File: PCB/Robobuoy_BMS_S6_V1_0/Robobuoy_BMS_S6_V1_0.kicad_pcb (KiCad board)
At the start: 4 copper layers, 147 parts, among them J101 Balance, J102 Balance, Q101 BFS20, Q102 MMBT5401, Q103 MMBT5401, Q104 MMBT5401, Q105 MMBT5401, Q106 MMBT5401, Q107 MMBT5401, Q108 MMBT5401, Q109 MMBT5401, Q110 MMBT5401, Q111 MMBT5401, Q112 MMBT5401, Q113 MMBT5401, Q114 BFS20, Q115 BFS20, Q116 HYG025N04NA1C2, Q117 HYG025N04NA1C2, Q118 HYG025N04NA1C2, Q119 HYG025N04NA1C2, U101 DW01A, U102 DW01A, U103 DW01A, U104 DW01A, U105 DW01A, U106 DW01A, U107 ETA3000D2I, U108 ETA3000D2I, U109 ETA3000D2I, U110 ETA3000D2I, U111 ETA3000D2I

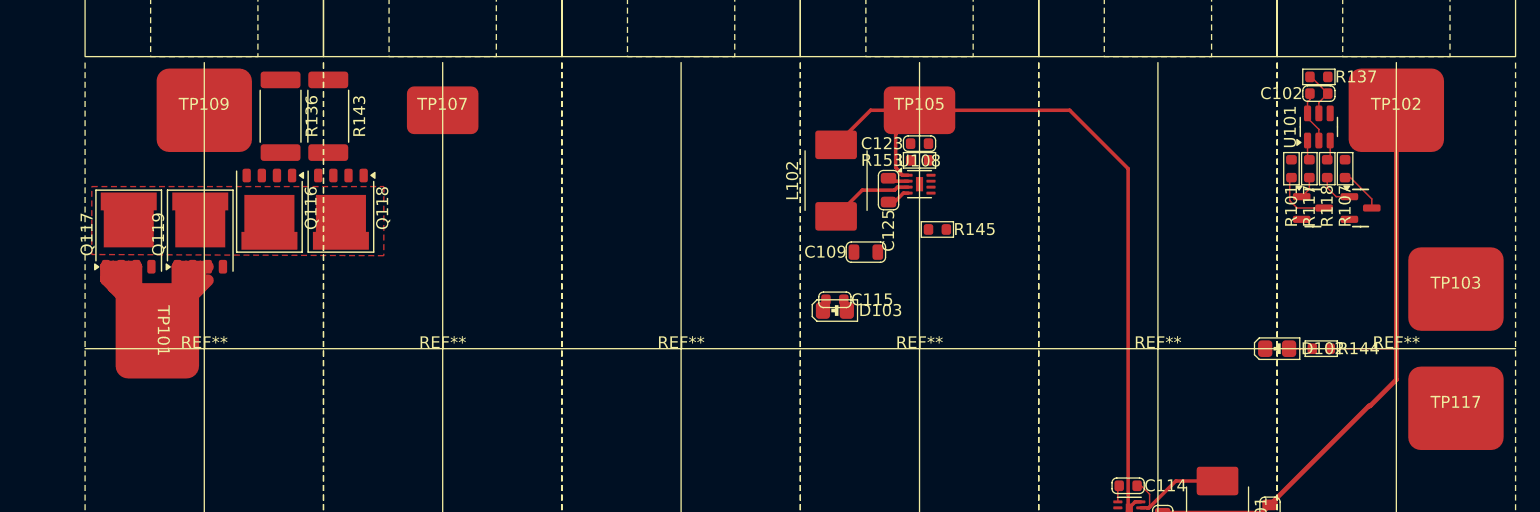
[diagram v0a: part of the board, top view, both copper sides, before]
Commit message: Schematics changed for singel board cpu/psu sub
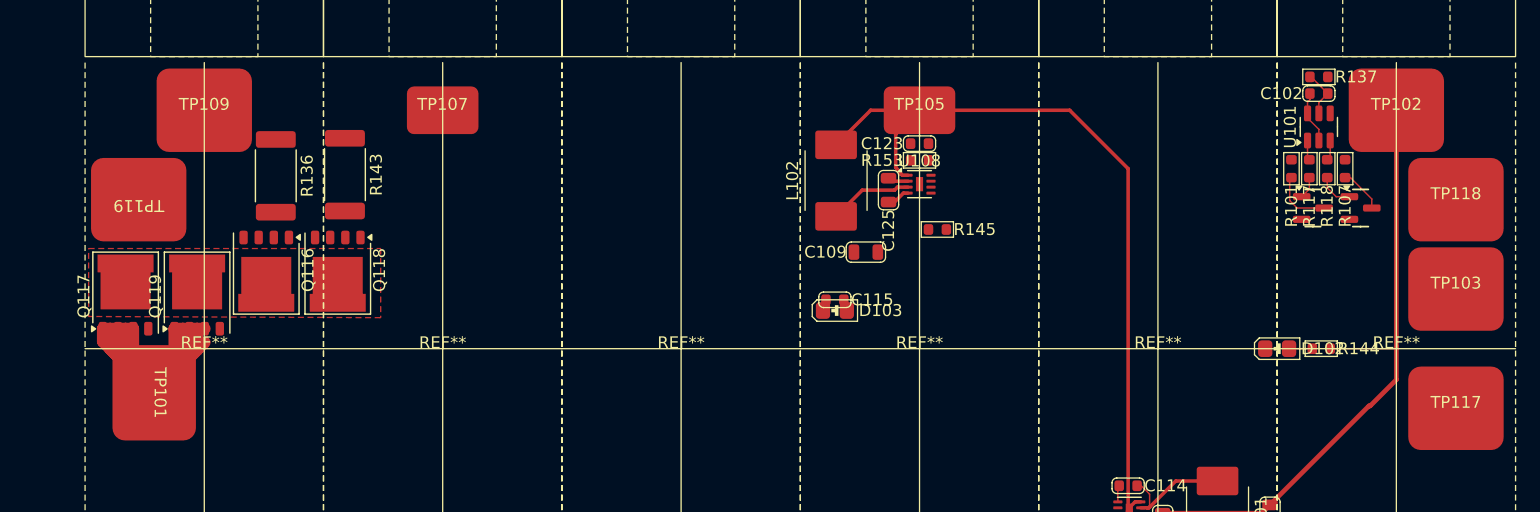
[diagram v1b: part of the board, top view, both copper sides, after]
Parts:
- added TP118: P+, A_Misc:TestPad_7x8, F.Cu at (165.0, 107.5)
- added TP119: B-, A_Misc:TestPad_7x8, F.Cu at (54.5, 107.5)
- moved TP101 5.21 mm to (55.8, 123.7)
- moved Q116 5.21 mm to (65.2, 113.4)
- moved Q118 5.21 mm to (71.2, 113.4)
- moved Q117 5.21 mm to (53.4, 115.6)
- moved Q119 5.21 mm to (59.4, 115.6)
- moved R143 5.10 mm to (71.8, 105.4)
- moved R136 5.02 mm to (66.0, 105.5)

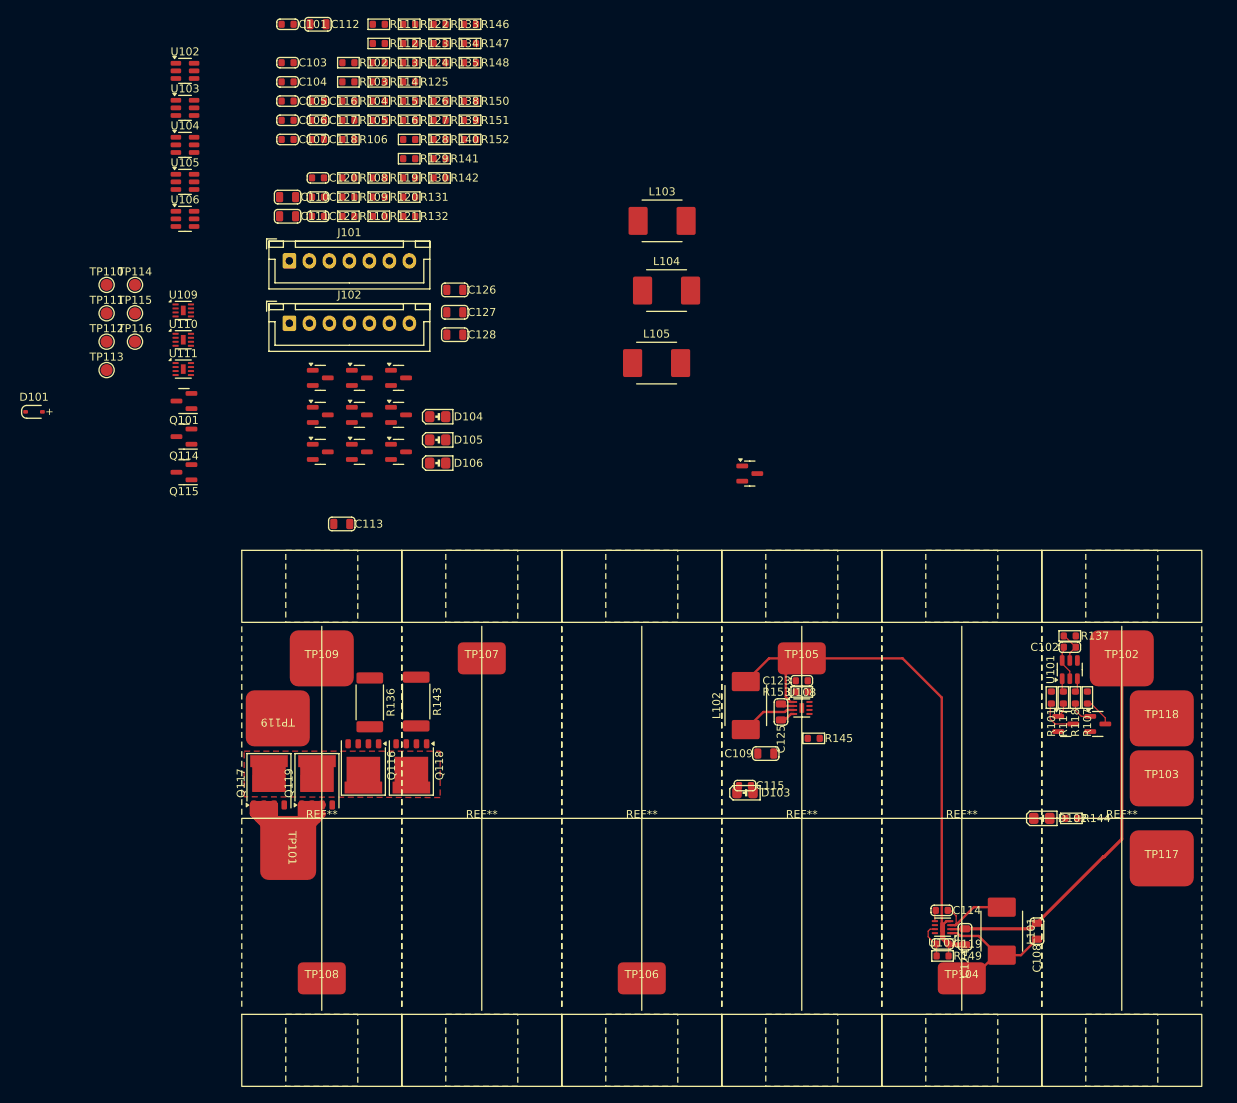
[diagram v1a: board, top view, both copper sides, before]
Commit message: Simulation added bms Little improvements BMS Resistor divider added on the gate of the mosfet (Limmeded to +/-20V could be 30V during charging)
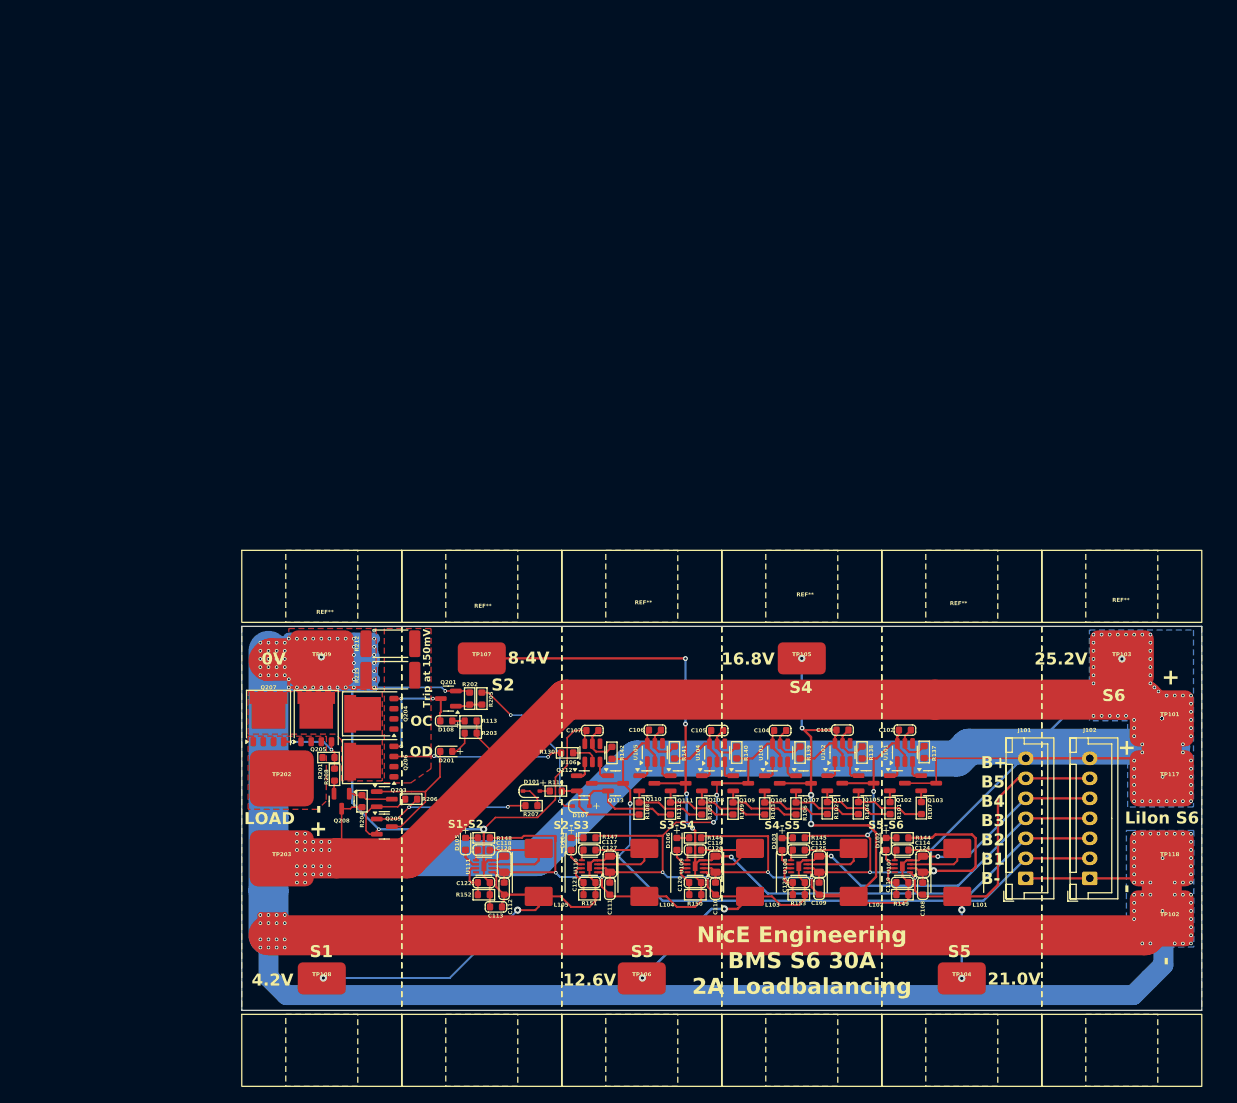
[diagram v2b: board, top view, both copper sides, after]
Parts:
- removed C101: 470nF, A_Device:C_0603
- removed Q101, Q114, Q115: BFS20, A_IC_SOT:SOT-23_jlc
- removed Q116, Q117, Q118, Q119: HYG025N04NA1C2, Package_DFN_QFN:PQFN-8-EP_6x5mm_P1.27mm_Generic
- removed R112, R114, R116, R117, R118, R119, R120, R121, R122, R123, R124, R125, R126, R127, R128, R129, R131, R132, R133, R135: 1M, A_Device:R_0603
- removed R115, R134: 10M, A_Device:R_0603
- removed R136, R143: R005, Resistor_SMD:R_2512_6332Metric_Pad1.40x3.35mm_HandSolder
- removed TP110: B+, TestPoint:TestPoint_Pad_D1.5mm
- removed TP111: B5, TestPoint:TestPoint_Pad_D1.5mm
- removed TP112: B4, TestPoint:TestPoint_Pad_D1.5mm
- removed TP113: B3, TestPoint:TestPoint_Pad_D1.5mm
- removed TP114: B2, TestPoint:TestPoint_Pad_D1.5mm
- removed TP115: B1, TestPoint:TestPoint_Pad_D1.5mm
- removed TP116: B-, TestPoint:TestPoint_Pad_D1.5mm
- removed TP119: B-, A_Misc:TestPad_7x8
- added D107: 1N4148WS, A_Device:D_SOD-323_1.8x1.4x1.15, F.Cu at (92.4, 118.5)
- added D108: RED, A_Device:LED_0603, F.Cu at (75.6, 107.8)
- added D201: RED, A_Device:LED_0603, F.Cu at (75.6, 111.6)
- added Q201: AO3400A, PCM_JLCPCB:Q_SOT-23, F.Cu at (75.8, 105.0)
- added Q203: AO3400A, PCM_JLCPCB:Q_SOT-23, F.Cu at (67.8, 117.6)
- added Q204: HYG025N04NA1C2, Package_DFN_QFN:PQFN-8-EP_6x5mm_P1.27mm_Generic, F.Cu at (66.3, 106.9)
- added Q205: HYG025N04NA1C2, Package_DFN_QFN:PQFN-8-EP_6x5mm_P1.27mm_Generic, F.Cu at (59.3, 107.7)
- added Q206: HYG025N04NA1C2, Package_DFN_QFN:PQFN-8-EP_6x5mm_P1.27mm_Generic, F.Cu at (66.3, 112.9)
- added Q207: HYG025N04NA1C2, Package_DFN_QFN:PQFN-8-EP_6x5mm_P1.27mm_Generic, F.Cu at (53.3, 107.7)
- added Q208: AO3400A, PCM_JLCPCB:Q_SOT-23, F.Cu at (62.5, 117.9)
- added Q209: AO3400A, PCM_JLCPCB:Q_SOT-23, F.Cu at (67.8, 121.0)
- added R201: 1M, A_Device:R_0603, F.Cu at (60.8, 112.4)
- added R202: 1M, A_Device:R_0603, F.Cu at (78.5, 105.0)
- added R203: 22K, A_Device:R_0603, F.Cu at (78.6, 109.3)
- added R204: 1M, A_Device:R_0603, F.Cu at (65.0, 117.9)
- added R205: 1K, A_Device:R_0603, F.Cu at (80.0, 105.0)
- added R206: 1M, A_Device:R_0603, F.Cu at (71.2, 117.6)
- added R207: 1K, A_Device:R_0603, F.Cu at (86.2, 118.4)
- added R208: 1M, A_Device:R_0603, F.Cu at (61.6, 114.5)
- added R212: R01, Resistor_SMD:R_2512_6332Metric_Pad1.40x3.35mm_HandSolder, F.Cu at (68.6, 98.2)
- added R213: R01, Resistor_SMD:R_2512_6332Metric_Pad1.40x3.35mm_HandSolder, F.Cu at (68.6, 102.1)
- added TP202: P-, A_Misc:TestPad_7x8, F.Cu at (55.0, 115.0)
- added TP203: P+, A_Misc:TestPad_7x8, F.Cu at (55.0, 125.0)
- C108, C109, C110, C111, C112, C113: footprint A_Device:C_0805 -> A_Device:C_0603
- D102: value 5-6 -> RED; footprint A_Passive:LED_0805 -> A_Device:LED_0603
- D103: value 4-5 -> RED; footprint A_Passive:LED_0805 -> A_Device:LED_0603
- D104: value 2-3 -> RED; footprint A_Passive:LED_0805 -> A_Device:LED_0603
- D105: value 1-2 -> RED; footprint A_Passive:LED_0805 -> A_Device:LED_0603
- D106: value 4-3 -> RED; footprint A_Passive:LED_0805 -> A_Device:LED_0603
- Q102, Q103, Q104, Q105, Q106, Q107, Q108, Q109, Q110, Q111, Q112, Q113: value MMBT5401 -> AO3400A
- R101, R102, R103, R104, R105, R106, R107, R108, R109, R110, R111: value 1M -> 1K
- R113: value 1M -> 22K
- R137, R138, R139, R140, R141, R142: value 1k -> 100
- R144, R145, R146, R147, R148: value 1k -> 1K
- R149, R150, R151, R152, R153: value 25K -> 24K
- TP101, TP117: value P- -> VBATT+
- TP102, TP118: value P+ -> VBATT-
- moved J102 121.8 mm to (156.0, 127.5), turned to 90 degrees
- moved J101 120.1 mm to (148.0, 127.5), turned to 90 degrees
- moved U102 118.4 mm to (125.1, 111.8), turned to 90 degrees
- moved TP101 111.4 mm to (166.0, 107.5), turned to 0 degrees
- moved R102 110.8 mm to (123.2, 118.7), turned to 90 degrees
- moved C112 110.5 mm to (82.8, 128.8), turned to -90 degrees
- moved U103 109.7 mm to (117.3, 111.8), turned to 90 degrees
- moved R104 109.0 mm to (127.1, 118.7), turned to 90 degrees
- moved C103 108.5 mm to (125.1, 109.0), turned to 180 degrees
- moved R146 105.5 mm to (106.7, 122.4)
- moved C116 104.8 mm to (106.7, 124.0)
- moved R103 104.7 mm to (115.4, 118.8), turned to 90 degrees
- moved R111 104.6 mm to (103.6, 118.8), turned to 90 degrees
- moved R150 103.1 mm to (106.7, 129.5)
- moved C104 101.8 mm to (117.3, 109.0), turned to 180 degrees
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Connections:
- D101 pad 1: Net-(D101-K) -> /Curren-Overcharge-Protection/OD
- Q102 pad 1: Net-(Q102-B) -> Net-(Q102-G)
- Q102 pad 2: VBATT+ -> Net-(Q102-S)
- Q102 pad 3: Net-(Q102-C) -> VBATT+
- Q103 pad 1: Net-(Q103-B) -> Net-(Q103-G)
- Q103 pad 2: VBATT+ -> Net-(Q103-S)
- Q103 pad 3: Net-(Q103-C) -> VBATT+
- Q104 pad 1: Net-(Q104-B) -> Net-(Q104-G)
- Q104 pad 2: /B5 -> Net-(Q104-S)
- Q104 pad 3: Net-(Q104-C) -> /B5
- Q105 pad 1: Net-(Q105-B) -> Net-(Q105-G)
- Q105 pad 2: /B5 -> Net-(Q105-S)
- Q105 pad 3: Net-(Q105-C) -> /B5
- Q106 pad 1: Net-(Q106-B) -> Net-(Q106-G)
- Q106 pad 2: /B4 -> Net-(Q106-S)
- Q106 pad 3: Net-(Q106-C) -> /B4
- Q107 pad 1: Net-(Q107-B) -> Net-(Q107-G)
- Q107 pad 2: /B4 -> Net-(Q107-S)
- Q107 pad 3: Net-(Q107-C) -> /B4
- Q108 pad 1: Net-(Q108-B) -> Net-(Q108-G)
- Q108 pad 2: /B3 -> Net-(Q108-S)
- Q108 pad 3: Net-(Q108-C) -> /B3
- Q109 pad 1: Net-(Q109-B) -> Net-(Q109-G)
- Q109 pad 2: /B3 -> Net-(Q109-S)
- Q109 pad 3: Net-(Q109-C) -> /B3
- Q110 pad 1: Net-(Q110-B) -> Net-(Q110-G)
- Q110 pad 2: /B2 -> Net-(Q110-S)
- Q110 pad 3: Net-(Q110-C) -> /B2
- Q111 pad 1: Net-(Q111-B) -> Net-(Q111-G)
- Q111 pad 2: /B2 -> Net-(Q111-S)
- Q111 pad 3: Net-(Q111-C) -> /B2
- Q112 pad 1: Net-(Q112-B) -> Net-(Q112-G)
- Q112 pad 2: /B1 -> Net-(Q112-S)
- Q112 pad 3: Net-(Q112-C) -> /B1
- Q113 pad 1: Net-(Q113-B) -> Net-(Q113-G)
- Q113 pad 2: /B1 -> Net-(D107-A)
- Q113 pad 3: Net-(Q113-C) -> /B1
- R101 pad 1: Net-(Q104-C) -> Net-(Q104-S)
- R101 pad 2: Net-(Q102-C) -> Net-(Q102-S)
- R102 pad 1: Net-(Q106-C) -> Net-(Q106-S)
- R102 pad 2: Net-(Q104-C) -> Net-(Q104-S)
- R103 pad 1: Net-(Q108-C) -> Net-(Q108-S)
- R103 pad 2: Net-(Q106-C) -> Net-(Q106-S)
- R104 pad 1: Net-(Q110-C) -> Net-(Q107-S)
- R104 pad 2: Net-(Q108-C) -> Net-(Q105-S)
- R105 pad 1: Net-(Q112-C) -> Net-(Q110-S)
- R105 pad 2: Net-(Q110-C) -> Net-(Q108-S)
- R106 pad 1: Net-(D101-A) -> Net-(Q109-S)
- R106 pad 2: Net-(Q112-C) -> Net-(Q107-S)
- R107 pad 1: Net-(Q105-C) -> Net-(Q105-S)
- R107 pad 2: Net-(Q103-C) -> Net-(Q103-S)
- R108 pad 1: Net-(Q107-C) -> Net-(Q112-S)
- R108 pad 2: Net-(Q105-C) -> Net-(Q110-S)
- R109 pad 1: Net-(Q109-C) -> Net-(Q111-S)
- R109 pad 2: Net-(Q107-C) -> Net-(Q109-S)
- R110 pad 1: Net-(Q111-C) -> Net-(D101-A)
- R110 pad 2: Net-(Q109-C) -> Net-(Q112-S)
- R111 pad 1: Net-(Q113-C) -> Net-(D107-A)
- R111 pad 2: Net-(Q111-C) -> Net-(Q111-S)
- R113 pad 1: VBATT- -> Net-(D108-A)
- R113 pad 2: Net-(Q101-B) -> VBATT+
- R130 pad 1: Net-(Q116-S-Pad1) -> /Curren-Overcharge-Protection/Vtrip
- TP101 pad 1: /P- -> VBATT+
- TP102 pad 1: VBATT+ -> VBATT-
- TP117 pad 1: /P- -> VBATT+
- TP118 pad 1: VBATT+ -> VBATT-
- U101 pad 1: Net-(U101-OD) -> Net-(Q102-G)
- U101 pad 3: Net-(U101-OC) -> Net-(Q103-G)
- U102 pad 1: Net-(U102-OD) -> Net-(Q104-G)
- U102 pad 3: Net-(U102-OC) -> Net-(Q105-G)
- U103 pad 1: Net-(U103-OD) -> Net-(Q106-G)
- U103 pad 3: Net-(U103-OC) -> Net-(Q107-G)
- U104 pad 1: Net-(U104-OD) -> Net-(Q108-G)
- U104 pad 3: Net-(U104-OC) -> Net-(Q109-G)
- U105 pad 1: Net-(U105-OD) -> Net-(Q110-G)
- U105 pad 3: Net-(U105-OC) -> Net-(Q111-G)
- U106 pad 1: Net-(U106-OD) -> Net-(Q112-G)
- U106 pad 3: Net-(U106-OC) -> Net-(Q113-G)
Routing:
- net VBATT-: track 0.00 -> 502.3 mm, vias 0 -> 117
- net VBATT+: track 54.3 -> 384.7 mm, vias 0 -> 93
- net /B2: track 0.00 -> 169.5 mm, vias 0 -> 7
- net /B1: track 0.00 -> 147.9 mm, vias 0 -> 4
- net /B3: track 1.95 -> 136.7 mm, vias 0 -> 7
- net /B5: track 25.2 -> 97.4 mm, vias 0 -> 6
- net /P-: track 70.2 -> 0.00 mm
- net /B4: track 70.9 -> 138.0 mm, vias 0 -> 7
- net /Curren-Overcharge-Protection/Vtrip: track 0.00 -> 21.2 mm, vias 0 -> 2
- net /Curren-Overcharge-Protection/OC: track 0.00 -> 20.7 mm, vias 0 -> 2
- net Net-(Q209-G): track 0.00 -> 20.7 mm, vias 0 -> 2
- net Net-(D201-K): track 0.00 -> 18.6 mm
- net Net-(D108-K): track 0.00 -> 15.6 mm, vias 0 -> 3
- net Net-(D107-A): track 0.00 -> 13.7 mm
- net Net-(U110-SW): track 0.00 -> 13.5 mm
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- added copper zone on F.Cu, net /Curren-Overcharge-Protection/P-
- added copper zone on F.Cu, net /Curren-Overcharge-Protection/Vtrip
- added copper zone on F.Cu, net Net-(Q204-D)
- added copper zone on B.Cu, net VBATT+
- added copper zone on In2.Cu, net VBATT+
- added copper zone on B.Cu, net VBATT-
- added copper zone on F.Cu, net VBATT-
- added copper zone on In1.Cu, net VBATT-
- removed copper zone on F.Cu, net Net-(Q116-D)
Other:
- board outline added: 120 x 48 mm
- board text added: "+"
- board text added: "-"
- board text added: "0V"
- board text added: "12.6V"
- board text added: "16.8V"
- board text added: "21.0V"
- board text added: "25.2V"
- board text added: "4.2V"
- board text added: "8.4V"
- board text added: "B+ B5 B4 B3 B2 B1 B-"
- board text added: "LOAD"
- board text added: "LiIon S6"
- board text added: "NicE Engineering BMS S6 30A 2A Active loadbalancing"
- board text added: "NicE Engineering BMS S6 30A 2A Loadbalancing"
- board text added: "S1"
- board text added: "S1-S2"
- board text added: "S2"
- board text added: "S2-S3"
- board text added: "S3"
- board text added: "S3-S4"
- board text added: "S4"
- board text added: "S4-S5"
- board text added: "S5"
- board text added: "S5-S6"
- board text added: "S6"
- board text added: "Trip at 150mV"

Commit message: PCB adjustmend Sub V3.0
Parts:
- added TP110: B1, A_Misc:TestPad_4x6, F.Cu at (76.6, 140.2)
- added TP111: B2, A_Misc:TestPad_4x6, F.Cu at (101.7, 99.3)
- added TP112: B3, A_Misc:TestPad_4x6, F.Cu at (120.0, 140.0)
- added TP113: B4, A_Misc:TestPad_4x6, F.Cu at (140.0, 100.0)
- added TP114: B5, A_Misc:TestPad_4x6, F.Cu at (160.0, 140.0)
- R208: value 1M -> 10K
- turned R208 to -90 degrees
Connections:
- R208 pad 1: Net-(Q208-S) -> Net-(Q205-G)
- R208 pad 2: Net-(Q205-G) -> Net-(Q208-S)
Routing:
- net /B5: track 97.4 -> 117.4 mm
- net /B4: track 138.0 -> 158.0 mm
- net /B3: track 136.7 -> 149.3 mm
- net /B1: track 147.9 -> 150.1 mm
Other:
- board text added: "0"
- board text added: "25.2V B+ B5 B4 B3 B2 B1 B- 0V"
- board text added: "BMS S6 30A / 2A Loadbalancing"
- board text added: "NicE Engineering"
- board text removed: "NicE Engineering BMS S6 30A 2A Loadbalancing"

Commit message: Small changes on pcb
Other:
- outline, holes or cut-outs redrawn
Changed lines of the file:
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@@
 			(disableapertmacros no)
 			(usegerberextensions no)
-			(usegerberattributes yes)
-			(usegerberadvancedattributes yes)
+			(usegerberattributes no)
+			(usegerberadvancedattributes no)
 			(creategerberjobfile yes)
 			(dashed_line_dash_ratio 12.000000)
@@
 			(outputformat 1)
 			(mirror no)
-			(drillshape 1)
+			(drillshape 0)
 			(scaleselection 1)
 			(outputdirectory "")
@@
 			(net 45 "unconnected-(U105-TD-Pad4)")
 			(pinfunction "TD")
-			(pintype "input")
+			(pintype "input+no_connect")
 		)
 		(pad "5" smd roundrect
@@
 			(net 43 "unconnected-(U103-TD-Pad4)")
 			(pinfunction "TD")
-			(pintype "input")
+			(pintype "input+no_connect")
 		)
 		(pad "5" smd roundrect
@@
 			(net 41 "unconnected-(U101-TD-Pad4)")
 			(pinfunction "TD")
-			(pintype "input")
+			(pintype "input+no_connect")
 		)
 		(pad "5" smd roundrect
@@
 		(sheetname "/")
 		(sheetfile "Robobuoy_BMS_S6_V1_0.kicad_sch")
-		(attr through_hole)
+		(attr through_hole dnp)
 		(fp_line
 			(start -1.6 -2.75)
@@
 			(net 44 "unconnected-(U104-TD-Pad4)")
 			(pinfunction "TD")
-			(pintype "input")
+			(pintype "input+no_connect")
 		)
 		(pad "5" smd roundrect
@@
 		(sheetname "/")
 		(sheetfile "Robobuoy_BMS_S6_V1_0.kicad_sch")
-		(attr through_hole)
+		(attr through_hole dnp)
 		(fp_line
 			(start -1.6 -2.75)
@@
 			)
 		)
-		(property "LCSC" "C25197"
+		(property "LCSC" ""
 			(at 0 0 270)
 			(unlocked yes)
@@
 			(net 42 "unconnected-(U102-TD-Pad4)")
 			(pinfunction "TD")
-			(pintype "input")
+			(pintype "input+no_connect")
 		)
 		(pad "5" smd roundrect
@@
 			(net 46 "unconnected-(U106-TD-Pad4)")
 			(pinfunction "TD")
-			(pintype "input")
+			(pintype "input+no_connect")
 		)
 		(pad "5" smd roundrect
@@
 	)
 	(gr_line
-		(start 50 96)
-		(end 170 96)
+		(start 51 96)
+		(end 169 96)
+		(stroke
+			(width 0.1)
+			(type default)
+		)
+		(layer "Edge.Cuts")
+	)
+	(gr_arc
+		(start 170 143)
+		(mid 169.707107 143.707107)
+		(end 169 144)
 		(stroke
 			(width 0.1)
@@
 	)
 	(gr_line
-		(start 170 144)
-		(end 50 144)
+		(start 169 144)
+		(end 51 144)
+		(stroke
+			(width 0.1)
+			(type default)
+		)
+		(layer "Edge.Cuts")
+	)
+	(gr_arc
+		(start 50 97)
+		(mid 50.292893 96.292893)
+		(end 51 96)
+		(stroke
+			(width 0.1)
+			(type default)
+		)
+		(layer "Edge.Cuts")
+	)
+	(gr_arc
+		(start 169 96)
+		(mid 169.707107 96.292893)
+		(end 170 97)
+		(stroke
+			(width 0.1)
+			(type default)
+		)
+		(layer "Edge.Cuts")
+	)
+	(gr_arc
+		(start 51 144)
+		(mid 50.292893 143.707107)
+		(end 50 143)
 		(stroke
 			(width 0.1)
@@
 	)
 	(gr_line
-		(start 170 96)
-		(end 170 144)
+		(start 170 97)
+		(end 170 143)
 		(stroke
 			(width 0.1)
@@
 	)
 	(gr_line
-		(start 50 144)
-		(end 50 96)
+		(start 50 143)
+		(end 50 97)
 		(stroke
 			(width 0.1)
@@
 	)
 	(gr_text "0V"
-		(at 54.356 97.282 0)
+		(at 51.5292 96.9876 0)
 		(layer "F.SilkS")
 		(effects
@@
 	)
 	(gr_text "25.2V"
-		(at 168.148 101.473 90)
+		(at 52.9008 129.6012 0)
 		(layer "F.SilkS")
 		(effects

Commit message: Heel veel AI veranderingen.
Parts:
- moved R207 2.27 mm to (84.0, 118.7)
- moved D101 0.44 mm to (85.8, 116.6)
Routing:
- net VBATT+: track 384.7 -> 456.5 mm
- net VBATT-: track 502.3 -> 545.8 mm
- net /B1: track 150.1 -> 146.5 mm
- net Net-(Q209-G): track 20.7 -> 18.4 mm
- net /B5: track 117.4 -> 115.9 mm
- net /Curren-Overcharge-Protection/OD: track 3.08 -> 2.09 mm
- net Net-(U111-SW): track 13.5 -> 12.6 mm
